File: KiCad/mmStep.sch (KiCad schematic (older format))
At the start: 20 parts, among them J1 Conn_02x08_Top_Bottom, J2 DX07S016JA1R1500, J3 MICROMOD-2222-C, J4 DEBUG, J5 I2C, J6 Screw_Terminal_01x02, SW1 SW_Push, SW2 SW_Push, U1 MIC5219-3.3YM5

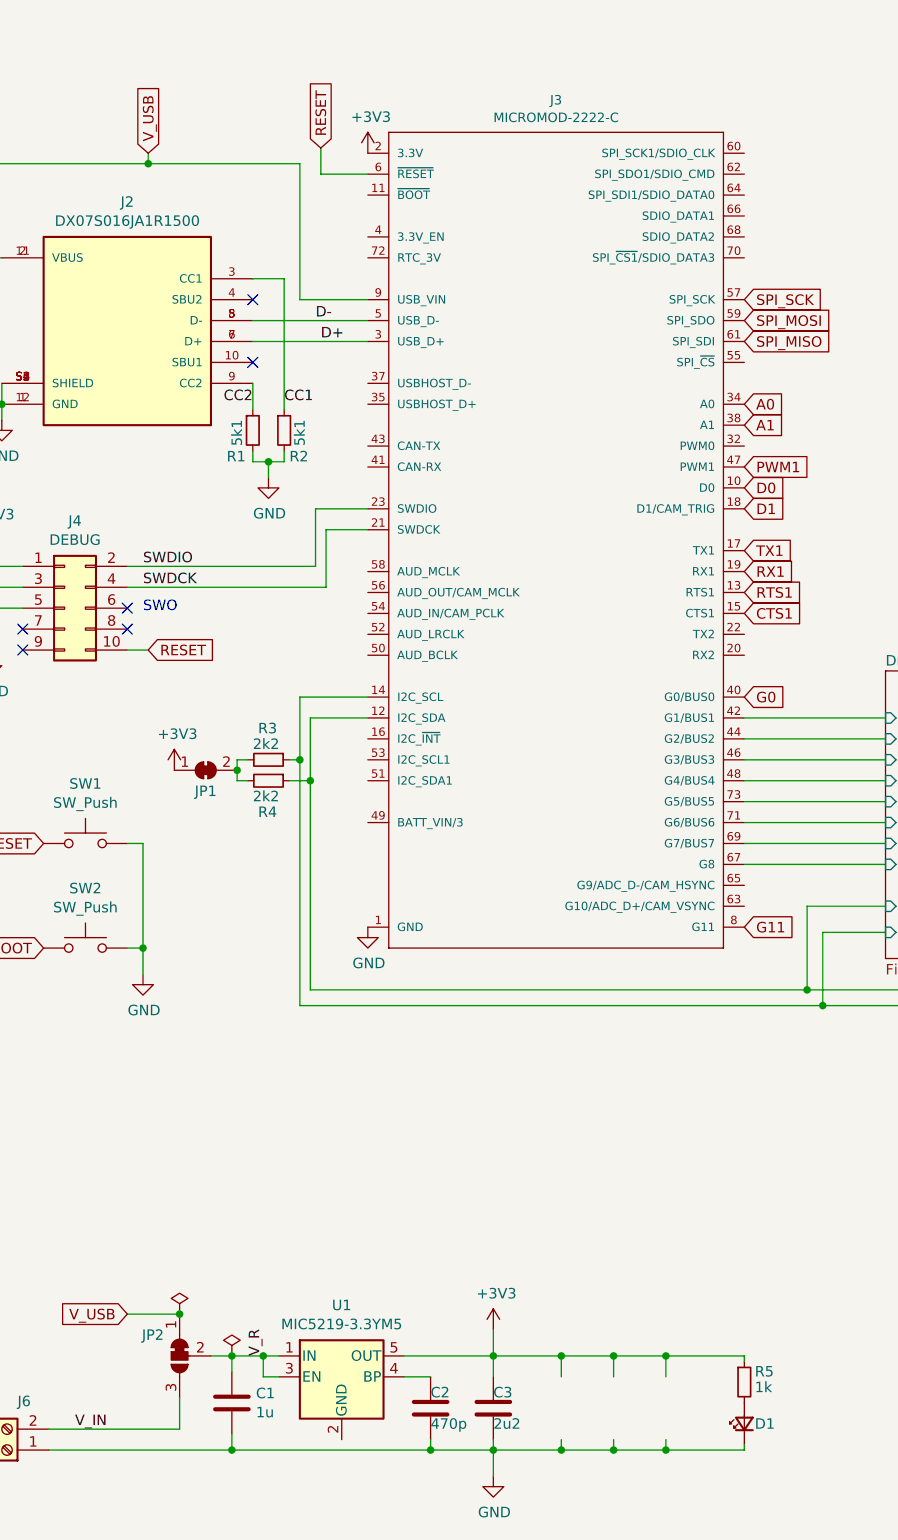
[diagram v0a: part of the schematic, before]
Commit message: Fixed missing BOOT signal and some ERC errors
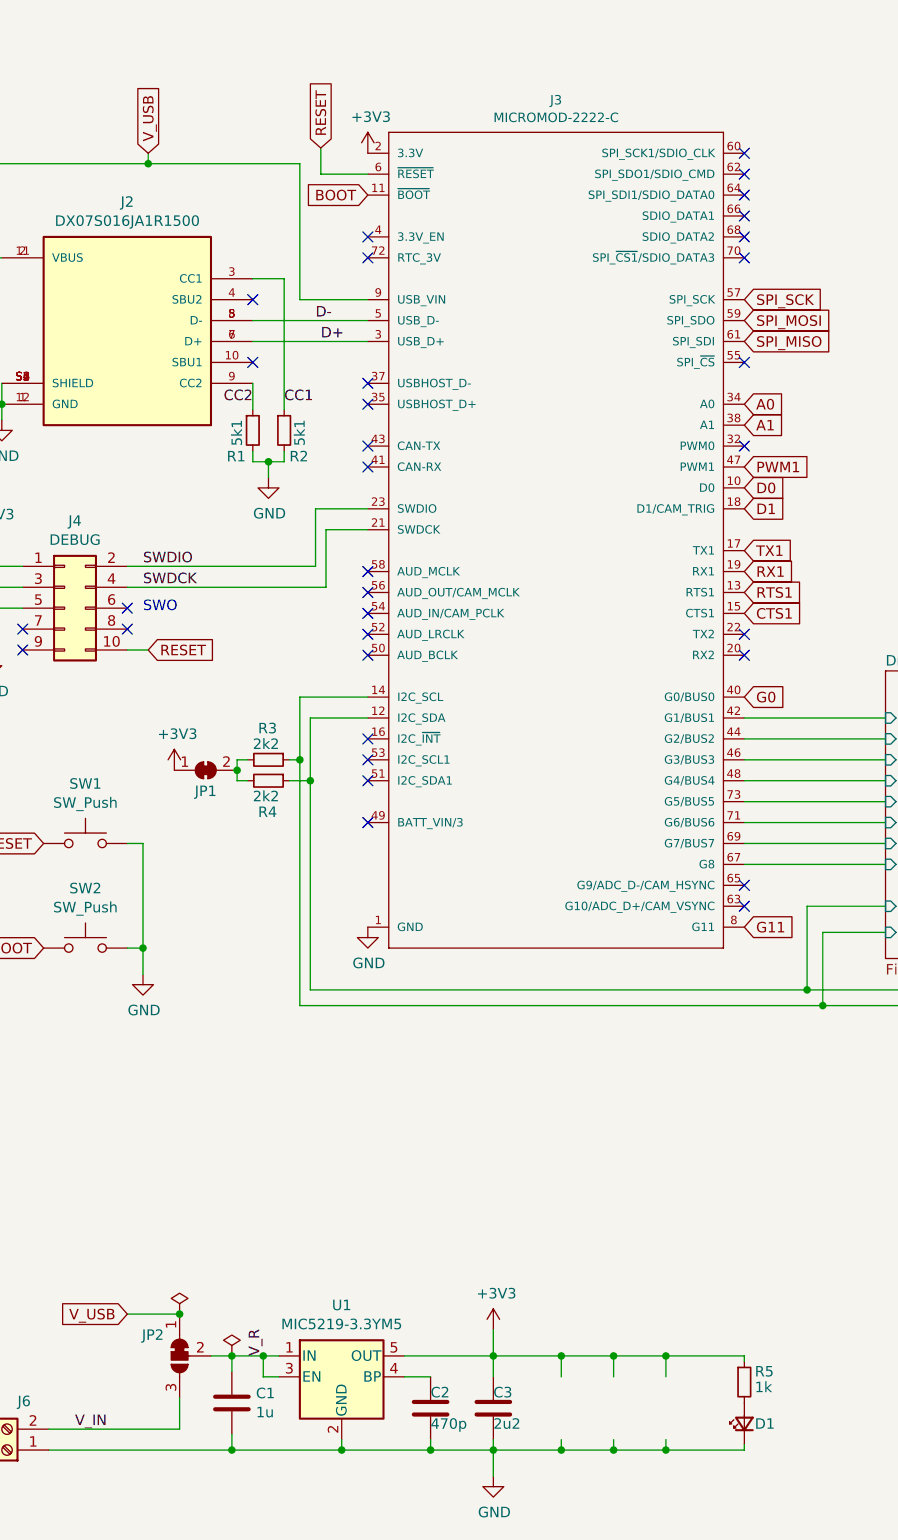
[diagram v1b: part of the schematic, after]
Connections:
- wire segments 107 -> 109
- no-connect marks 6 -> 33
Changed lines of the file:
@@
 	4125 7250 4125 7200
 Wire Wire Line
-	2050 7250 3000 7250
+	2050 7250 2575 7250
 Wire Wire Line
 	3875 7200 3875 7250
@@
 Wire Wire Line
 	2375 1750 2375 1100
-Wire Wire Line
-	2375 1100 1650 1100
 Wire Wire Line
 	900  1100 900  1550
@@
 Wire Wire Line
 	4500 4050 5175 4050
+NoConn ~ 2700 1450
+NoConn ~ 2700 1550
+NoConn ~ 2700 2150
+NoConn ~ 2700 2250
+NoConn ~ 2700 2450
+NoConn ~ 2700 2550
+NoConn ~ 2700 3050
+NoConn ~ 2700 3150
+NoConn ~ 2700 3250
+NoConn ~ 2700 3350
+NoConn ~ 2700 3450
+NoConn ~ 2700 3850
+NoConn ~ 2700 3950
+NoConn ~ 2700 4050
+NoConn ~ 2700 4250
+NoConn ~ 4500 2450
+NoConn ~ 4500 1050
+NoConn ~ 4500 1150
+NoConn ~ 4500 1250
+NoConn ~ 4500 1350
+NoConn ~ 4500 1450
+NoConn ~ 4500 1550
+NoConn ~ 4500 2050
+NoConn ~ 4500 3350
+NoConn ~ 4500 3450
+NoConn ~ 4500 4550
+NoConn ~ 4500 4650
+Text GLabel 2700 1250 0    50   Input ~ 0
+BOOT
+Wire Wire Line
+	2575 7200 2575 7250
+Connection ~ 2575 7250
+Wire Wire Line
+	2575 7250 3000 7250
+Wire Wire Line
+	1650 1100 2375 1100
 $EndSCHEMATC
